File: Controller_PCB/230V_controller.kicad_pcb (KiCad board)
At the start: 2 copper layers, 85 x 106.5 mm, 38 parts, among them J1 Screw_Terminal_01x02, J2 Screw_Terminal_01x02, J3 Screw_Terminal_01x02, J4 Screw_Terminal_01x02, K1 HF32FA, K2 HF32FA, Q1 BC546, Q2 BC546, Q3 BT136-600, Q4 BC546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

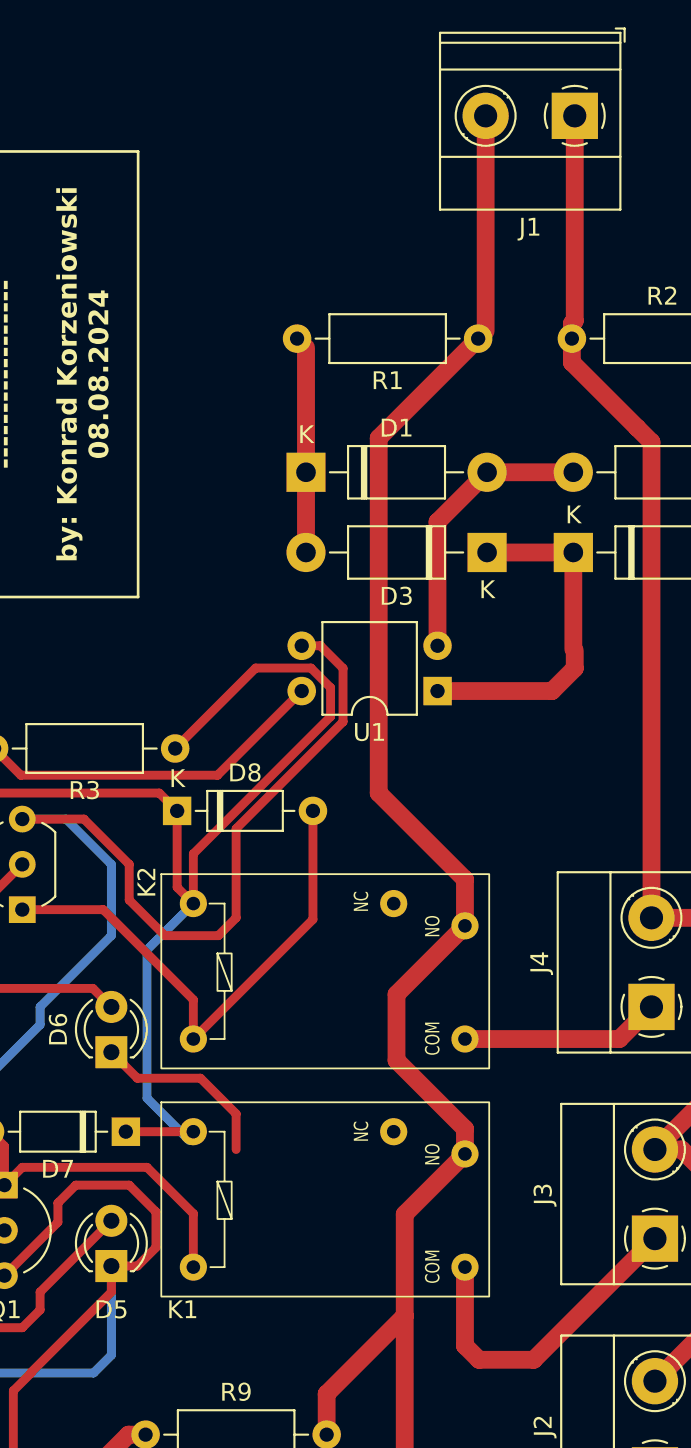
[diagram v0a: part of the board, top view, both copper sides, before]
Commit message: General update 1. Updated PCB traces (little fix to make them more straight), 2. Updated Gerber Files, 3. Removed GND zone in the Mains Voltage part of PCB to make it more secure, 4. Updated README.md (removed PCB pictures).
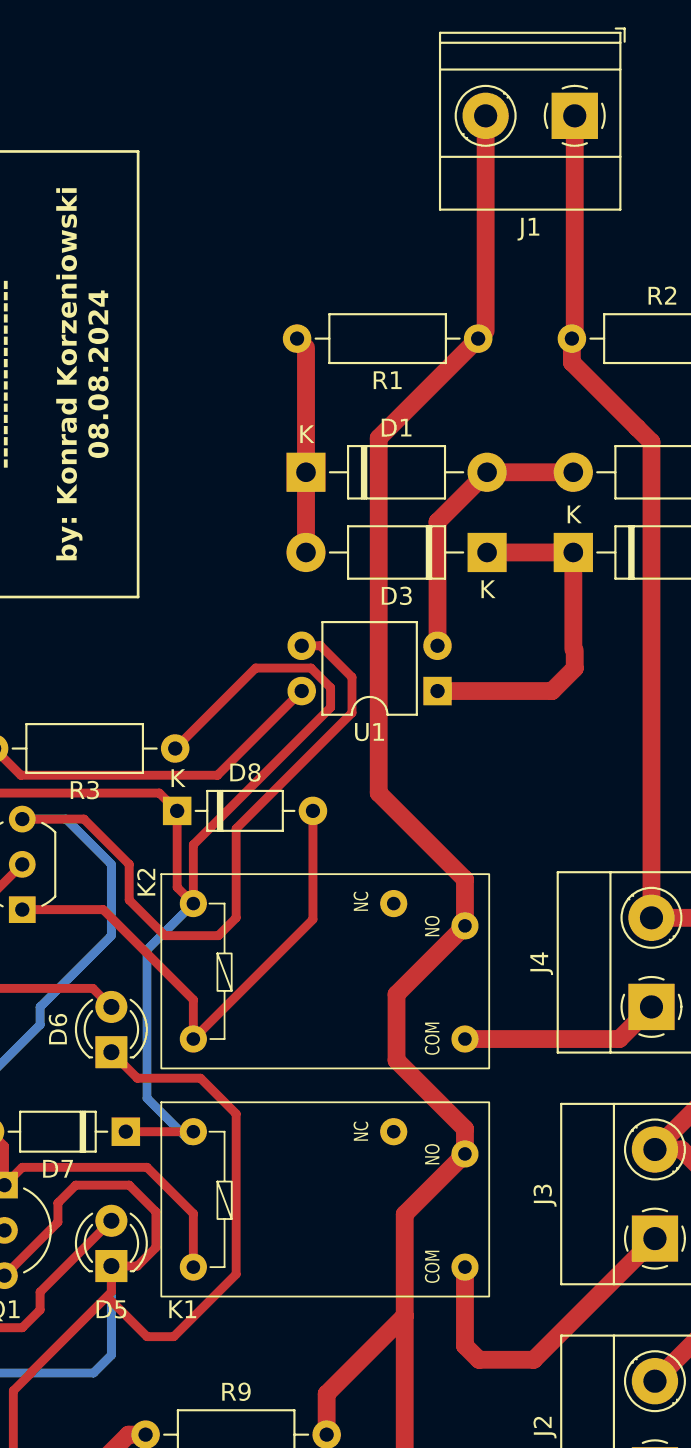
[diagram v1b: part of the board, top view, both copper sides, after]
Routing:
- net GND: track 351.8 -> 368.4 mm
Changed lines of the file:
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@@
 			(outputformat 1)
 			(mirror no)
-			(drillshape 1)
+			(drillshape 0)
 			(scaleselection 1)
-			(outputdirectory "")
+			(outputdirectory "D:/Dev/Mains-Voltage-Device-Controller/Controller_PCB/GerberFiles/")
 		)
 	)
@@
 	)
 	(segment
+		(start 214.46 93.46)
+		(end 211 93.46)
+		(width 0.5)
+		(layer "F.Cu")
+		(net 20)
+	)
+	(segment
+		(start 217.46 108)
+		(end 221 108)
+		(width 0.5)
+		(layer "F.Cu")
+		(net 20)
+	)
+	(segment
 		(start 188 79.31)
 		(end 188 56)
@@
 	)
 	(segment
+		(start 217 96)
+		(end 214.46 93.46)
+		(width 0.5)
+		(layer "F.Cu")
+		(net 20)
+	)
+	(segment
+		(start 222 100)
+		(end 219 100)
+		(width 0.5)
+		(layer "F.Cu")
+		(net 20)
+	)
+	(segment
 		(start 207 133)
 		(end 207 135)
@@
 	)
 	(segment
+		(start 229.5 85.5)
+		(end 229.5 87.5)
+		(width 0.5)
+		(layer "F.Cu")
+		(net 20)
+	)
+	(segment
+		(start 229.5 87.5)
+		(end 223 94)
+		(width 0.5)
+		(layer "F.Cu")
+		(net 20)
+	)
+	(segment
 		(start 211.5 124.5)
 		(end 216 120)
@@
 	)
 	(segment
-		(start 229 85)
-		(end 229 88)
+		(start 223 110)
+		(end 223 119)
 		(width 0.5)
 		(layer "F.Cu")
@@
 	)
 	(segment
+		(start 218 122.5)
+		(end 216 120.5)
+		(width 0.5)
+		(layer "F.Cu")
+		(net 20)
+	)
+	(segment
 		(start 183.5 107)
 		(end 181 107)
@@
 	)
 	(segment
-		(start 210.5 125.54)
-		(end 211.5 124.54)
+		(start 227.735 83.735)
+		(end 229.5 85.5)
 		(width 0.5)
 		(layer "F.Cu")
@@
 	)
 	(segment
-		(start 223 110)
-		(end 221 108)
+		(start 210.5 125.54)
+		(end 211.5 124.54)
 		(width 0.5)
 		(layer "F.Cu")
@@
 	)
 	(segment
-		(start 217 96)
-		(end 214.46 93.46)
+		(start 219.5 122.5)
+		(end 218 122.5)
 		(width 0.5)
 		(layer "F.Cu")
@@
 	)
 	(segment
-		(start 219 100)
-		(end 217 98)
-		(width 0.5)
-		(layer "F.Cu")
-		(net 20)
-	)
-	(segment
 		(start 192.76 143)
 		(end 191.54 141.78)
@@
 	)
 	(segment
-		(start 216 120)
-		(end 216 118.54)
+		(start 223 94)
+		(end 223 99)
 		(width 0.5)
 		(layer "F.Cu")
@@
 	)
 	(segment
-		(start 223 99)
-		(end 222 100)
+		(start 216 120)
+		(end 216 118.54)
 		(width 0.5)
 		(layer "F.Cu")
@@
 	)
 	(segment
-		(start 223 112)
-		(end 223 110)
-		(width 0.5)
-		(layer "F.Cu")
-		(net 20)
-	)
-	(segment
 		(start 197 143)
 		(end 207 133)
@@
 	)
 	(segment
-		(start 214.46 93.46)
-		(end 211 93.46)
+		(start 217 98)
+		(end 217 96)
 		(width 0.5)
 		(layer "F.Cu")
@@
 	)
 	(segment
-		(start 222 100)
-		(end 219 100)
-		(width 0.5)
-		(layer "F.Cu")
-		(net 20)
-	)
-	(segment
-		(start 217.46 108)
-		(end 216 106.54)
-		(width 0.5)
-		(layer "F.Cu")
-		(net 20)
-	)
-	(segment
-		(start 229 88)
-		(end 223 94)
-		(width 0.5)
-		(layer "F.Cu")
-		(net 20)
-	)
-	(segment
 		(start 183.5 101)
 		(end 181 101)
@@
 	)
 	(segment
-		(start 227.735 83.735)
-		(end 229 85)
-		(width 0.5)
-		(layer "F.Cu")
-		(net 20)
-	)
-	(segment
 		(start 186 101)
 		(end 183.5 101)
@@
 	)
 	(segment
-		(start 223 94)
-		(end 223 99)
-		(width 0.5)
-		(layer "F.Cu")
-		(net 20)
-	)
-	(segment
 		(start 217 142)
 		(end 217 135)
@@
 	)
 	(segment
-		(start 226.68 83.735)
-		(end 227.735 83.735)
-		(width 0.5)
-		(layer "F.Cu")
-		(net 20)
-	)
-	(segment
 		(start 177 90)
 		(end 178 91)
@@
 	)
 	(segment
+		(start 226.68 83.735)
+		(end 227.735 83.735)
+		(width 0.5)
+		(layer "F.Cu")
+		(net 20)
+	)
+	(segment
+		(start 216 106.54)
+		(end 217.46 108)
+		(width 0.5)
+		(layer "F.Cu")
+		(net 20)
+	)
+	(segment
 		(start 187.355 147)
 		(end 181.355 141)
@@
 	)
 	(segment
-		(start 217 98)
-		(end 217 96)
+		(start 223 99)
+		(end 222 100)
 		(width 0.5)
 		(layer "F.Cu")
@@
 	)
 	(segment
+		(start 219 100)
+		(end 217 98)
+		(width 0.5)
+		(layer "F.Cu")
+		(net 20)
+	)
+	(segment
 		(start 178 91)
 		(end 179.37 91)
@@
 	)
 	(segment
-		(start 218.5 117.5)
-		(end 217.46 118.54)
+		(start 221 108)
+		(end 223 110)
 		(width 0.5)
 		(layer "F.Cu")
@@
 	)
 	(segment
-		(start 221 108)
-		(end 217.46 108)
+		(start 223 119)
+		(end 219.5 122.5)
+		(width 0.5)
+		(layer "F.Cu")
+		(net 20)
+	)
+	(segment
+		(start 218.5 117.5)
+		(end 217.46 118.54)
 		(width 0.5)
 		(layer "F.Cu")
@@
 	)
 	(segment
+		(start 220.6 94.9)
+		(end 228.3 87.2)
+		(width 0.5)
+		(layer "F.Cu")
+		(net 25)
+	)
+	(segment
 		(start 216.81 111)
 		(end 220.6 111)
@@
 	(segment
 		(start 220.6 98.2)
-		(end 220.6 95.41005)
+		(end 220.6 94.9)
 		(width 0.5)
 		(layer "F.Cu")
@@
 	)
 	(segment
-		(start 220.6 95.41005)
-		(end 228.3 87.71005)
-		(width 0.5)
-		(layer "F.Cu")
-		(net 25)
-	)
-	(segment
-		(start 228.3 87.71005)
-		(end 228.3 86.087233)
+		(start 228.3 86.087233)
+		(end 227.197767 84.985)
 		(width 0.5)
 		(layer "F.Cu")
@@
 	)
 	(segment
-		(start 228.3 86.087233)
-		(end 227.197767 84.985)
+		(start 219.69 93)
+		(end 219.69 97.29)
 		(width 0.5)
 		(layer "F.Cu")
@@
 	)
 	(segment
-		(start 219.69 93)
-		(end 219.69 97.29)
+		(start 228.3 87.2)
+		(end 228.3 86.087233)
 		(width 0.5)
 		(layer "F.Cu")
@@
 	(segment
 		(start 241.84 66.5)
-		(end 241.84 65.66)
+		(end 242 66.34)
+		(width 1)
+		(layer "F.Cu")
+		(net 40)
+	)
+	(segment
+		(start 242 66.34)
+		(end 242 54)
 		(width 1)
 		(layer "F.Cu")
@@
 	)
 	(segment
-		(start 241.84 65.66)
-		(end 242 65.5)
-		(width 1)
-		(layer "F.Cu")
-		(net 40)
-	)
-	(segment
 		(start 246.305 99)
 		(end 249 99)
@@
 	)
 	(segment
-		(start 242 65.5)
-		(end 242 54)
-		(width 1)
-		(layer "F.Cu")
-		(net 40)
-	)
-	(segment
 		(start 250 121.5)
 		(end 250 114)
@@
 			)
 		)
+	)
+	(zone
+		(net 0)
+		(net_name "")
+		(layers "F&B.Cu")
+		(name "NoGND")
+		(hatch edge 0.5)
+		(connect_pads
+			(clearance 0)
+		)
+		(min_thickness 0.25)
+		(filled_areas_thickness no)
+		(keepout
+			(tracks allowed)
+			(vias allowed)
+			(pads allowed)
+			(copperpour not_allowed)
+			(footprints allowed)
+		)
+		(fill
+			(thermal_gap 0.5)
+			(thermal_bridge_width 0.5)
+		)
+		(polygon
+			(pts
+				(xy 258 42) (xy 258 148) (xy 209.5 148) (xy 209.5 124.5) (xy 223.5 124.5) (xy 223.5 42)
+			)
+		)
